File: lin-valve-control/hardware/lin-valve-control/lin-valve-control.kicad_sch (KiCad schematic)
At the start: 27 parts, among them J1 QWIIC Connector, J2 DIN-5_180degree, J3 DIN-5_180degree, J4 Screw_Terminal_01x02, J5 Screw_Terminal_01x03, J6 Screw_Terminal_01x03, Q1 2N7002, Q2 2N7002, U1 Arduino_Nano_v3.x, U2 TJA1021T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

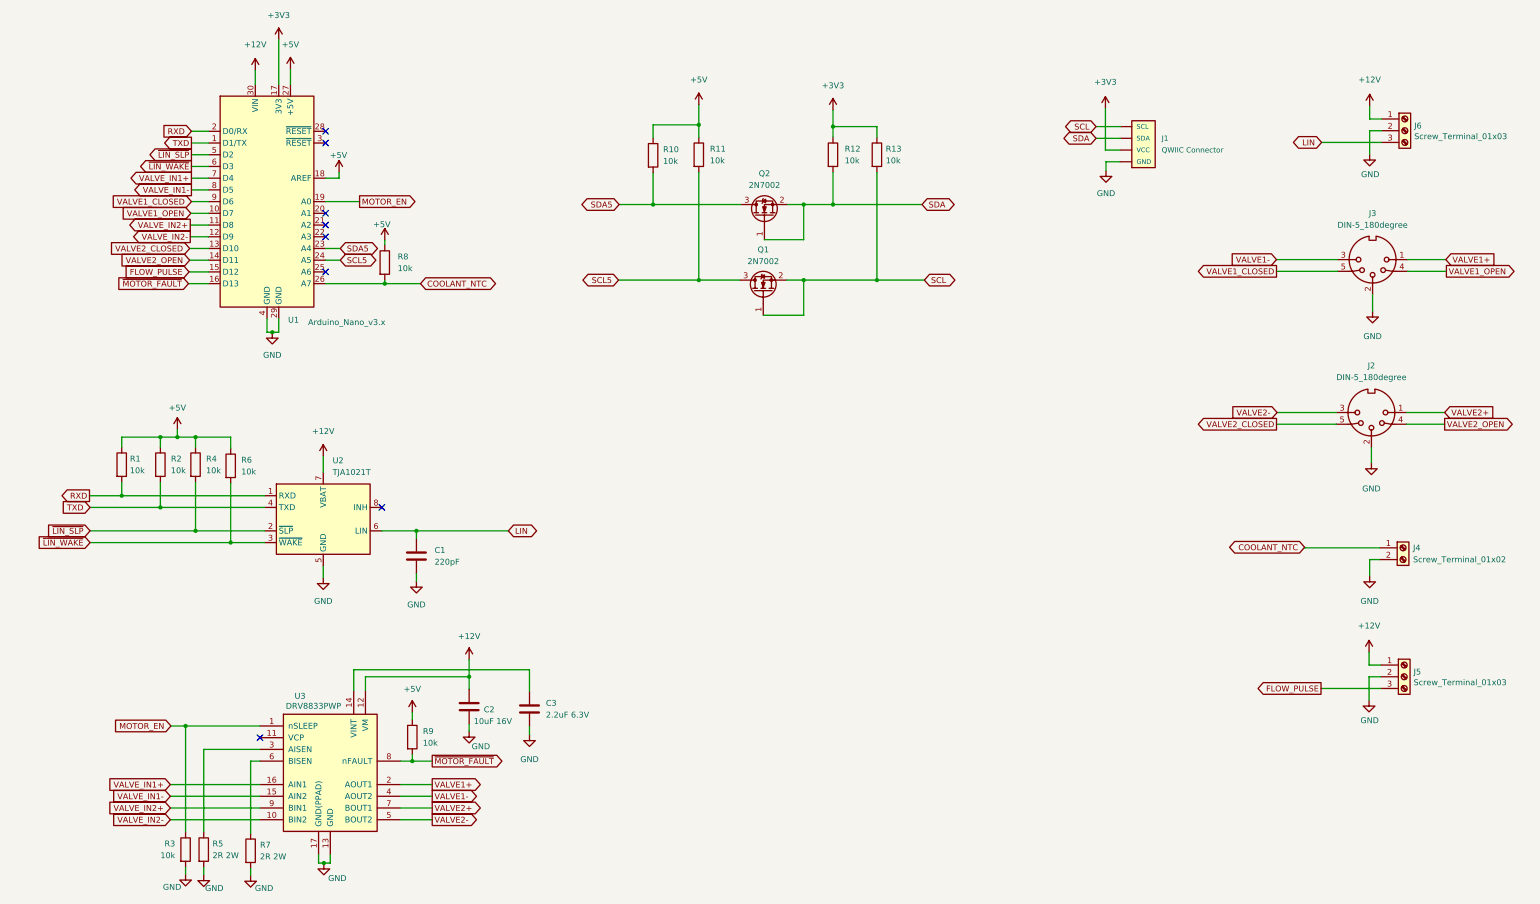
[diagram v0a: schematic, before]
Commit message: Move flow sensor to ICP1, run it at 5V
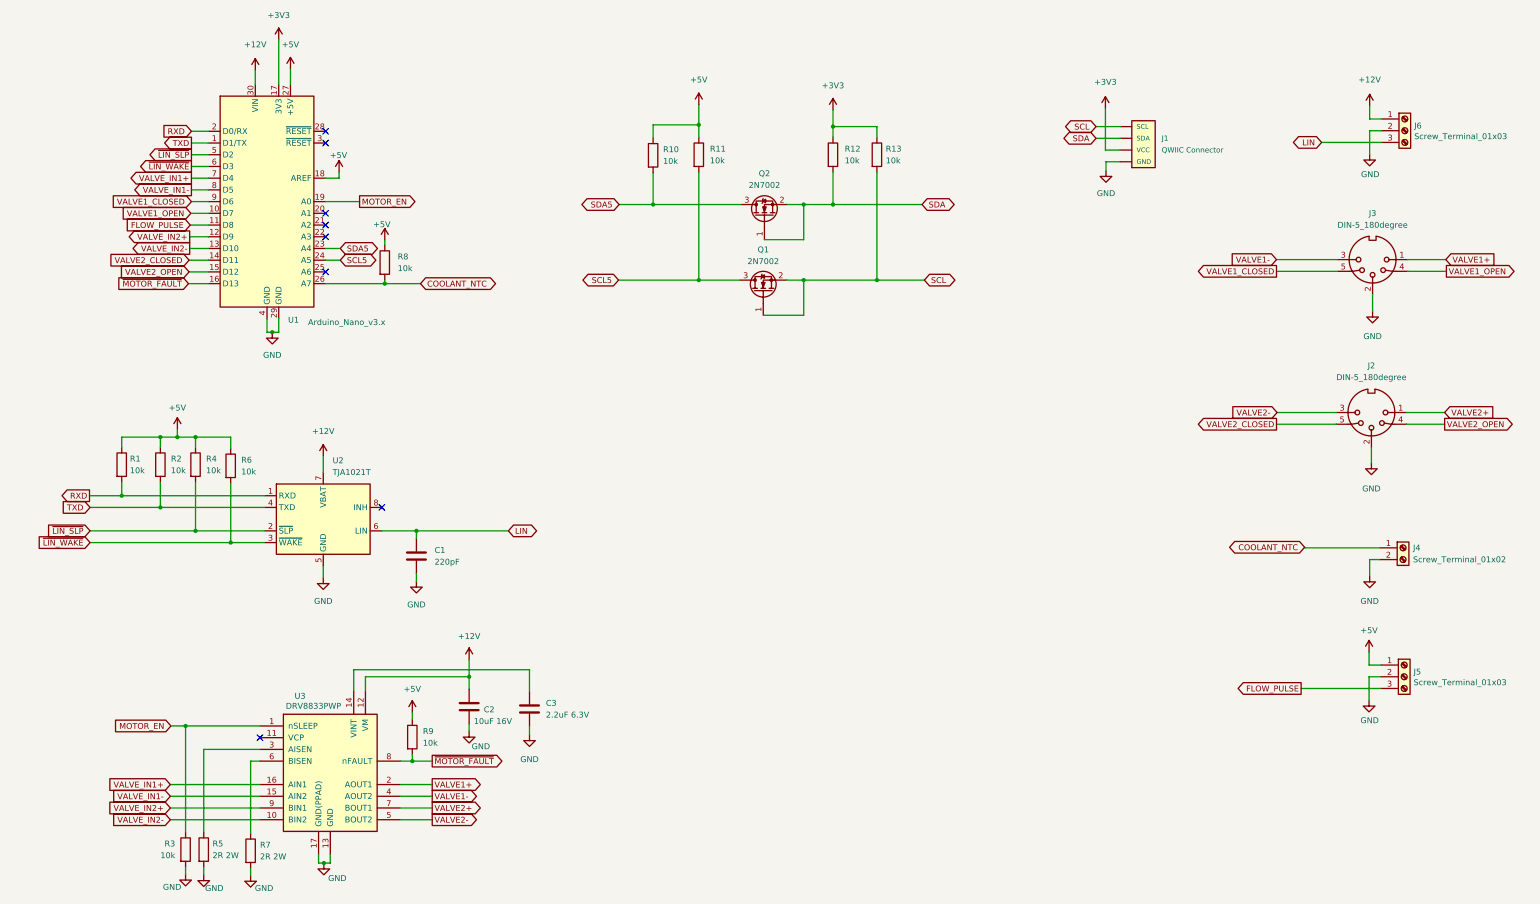
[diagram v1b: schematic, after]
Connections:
- net +12V: no longer J5.1 (Pin_1)
- net +5V: now also J5.1 (Pin_1)
- net FLOW_PULSE: now also U1.11 (D8); no longer U1.15 (D12)
- net VALVE2_CLOSED: now also U1.14 (D11); no longer U1.13 (D10)
- net VALVE2_OPEN: now also U1.15 (D12); no longer U1.14 (D11)
- net VALVE_IN2+: now also U1.12 (D9); no longer U1.11 (D8)
- net VALVE_IN2-: now also U1.13 (D10); no longer U1.12 (D9)
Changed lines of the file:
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@@
+    (stroke (width 0) (type default) (color 0 0 0 0))
+  )
+  (wire (pts (xy 48.387 67.056) (xy 52.578 67.056))
     (stroke (width 0) (type default) (color 0 0 0 0))
   )
@@
     (stroke (width 0) (type default) (color 0 0 0 0))
   )
-  (wire (pts (xy 48.641 61.976) (xy 52.578 61.976))
-    (stroke (width 0) (type default) (color 0 0 0 0))
-  )
   (wire (pts (xy 158.877 40.386) (xy 158.877 37.719))
     (stroke (width 0) (type default) (color 0 0 0 0))
@@
     (stroke (width 0) (type default) (color 0 0 0 0))
   )
-  (wire (pts (xy 306.705 159.893) (xy 293.751 159.893))
+  (wire (pts (xy 48.514 61.976) (xy 52.578 61.976))
     (stroke (width 0) (type default) (color 0 0 0 0))
   )
@@
     (stroke (width 0) (type default) (color 0 0 0 0))
   )
-  (wire (pts (xy 48.514 67.056) (xy 52.578 67.056))
-    (stroke (width 0) (type default) (color 0 0 0 0))
-  )
   (wire (pts (xy 48.895 39.116) (xy 52.578 39.116))
     (stroke (width 0) (type default) (color 0 0 0 0))
@@
   )
   (wire (pts (xy 77.978 49.276) (xy 80.899 49.276))
+    (stroke (width 0) (type default) (color 0 0 0 0))
+  )
+  (wire (pts (xy 289.433 159.893) (xy 306.705 159.893))
     (stroke (width 0) (type default) (color 0 0 0 0))
   )
@@
     )
   )
-  (global_label "VALVE_IN2-" (shape output) (at 48.641 61.976 180) (fields_autoplaced)
-    (effects (font (size 1.27 1.27)) (justify right))
-    (property "Intersheet References" "${INTERSHEET_REFS}" (id 0) (at 35.1892 61.8966 0)
+  (global_label "VALVE_IN2-" (shape output) (at 48.514 64.516 180) (fields_autoplaced)
+    (effects (font (size 1.27 1.27)) (justify right))
+    (property "Intersheet References" "${INTERSHEET_REFS}" (id 0) (at 35.0622 64.4366 0)
       (effects (font (size 1.27 1.27)) (justify right) hide)
     )
@@
     )
   )
-  (global_label "VALVE2_OPEN" (shape input) (at 48.514 67.056 180) (fields_autoplaced)
-    (effects (font (size 1.27 1.27)) (justify right))
-    (property "Intersheet References" "${INTERSHEET_REFS}" (id 0) (at 33.4898 66.9766 0)
+  (global_label "VALVE2_OPEN" (shape input) (at 48.387 69.596 180) (fields_autoplaced)
+    (effects (font (size 1.27 1.27)) (justify right))
+    (property "Intersheet References" "${INTERSHEET_REFS}" (id 0) (at 33.3628 69.5166 0)
       (effects (font (size 1.27 1.27)) (justify right) hide)
     )
@@
     )
   )
-  (global_label "VALVE2_CLOSED" (shape input) (at 48.514 64.516 180) (fields_autoplaced)
-    (effects (font (size 1.27 1.27)) (justify right))
-    (property "Intersheet References" "${INTERSHEET_REFS}" (id 0) (at 31.3127 64.4366 0)
+  (global_label "VALVE2_CLOSED" (shape input) (at 48.387 67.056 180) (fields_autoplaced)
+    (effects (font (size 1.27 1.27)) (justify right))
+    (property "Intersheet References" "${INTERSHEET_REFS}" (id 0) (at 31.1857 66.9766 0)
       (effects (font (size 1.27 1.27)) (justify right) hide)
     )
@@
     )
   )
-  (global_label "FLOW_PULSE" (shape input) (at 48.387 69.596 180) (fields_autoplaced)
-    (effects (font (size 1.27 1.27)) (justify right))
-    (property "Intersheet References" "${INTERSHEET_REFS}" (id 0) (at 34.2095 69.5166 0)
+  (global_label "FLOW_PULSE" (shape input) (at 48.641 59.436 180) (fields_autoplaced)
+    (effects (font (size 1.27 1.27)) (justify right))
+    (property "Intersheet References" "${INTERSHEET_REFS}" (id 0) (at 34.4635 59.3566 0)
       (effects (font (size 1.27 1.27)) (justify right) hide)
     )
@@
     )
   )
-  (global_label "VALVE_IN2+" (shape output) (at 48.641 59.436 180) (fields_autoplaced)
-    (effects (font (size 1.27 1.27)) (justify right))
-    (property "Intersheet References" "${INTERSHEET_REFS}" (id 0) (at 35.1892 59.3566 0)
+  (global_label "VALVE_IN2+" (shape output) (at 48.514 61.976 180) (fields_autoplaced)
+    (effects (font (size 1.27 1.27)) (justify right))
+    (property "Intersheet References" "${INTERSHEET_REFS}" (id 0) (at 35.0622 61.8966 0)
       (effects (font (size 1.27 1.27)) (justify right) hide)
     )
@@
     )
   )
-  (global_label "FLOW_PULSE" (shape output) (at 293.751 159.893 180) (fields_autoplaced)
-    (effects (font (size 1.27 1.27)) (justify right))
-    (property "Intersheet References" "${INTERSHEET_REFS}" (id 0) (at 279.5735 159.8136 0)
+  (global_label "FLOW_PULSE" (shape output) (at 289.433 159.893 180) (fields_autoplaced)
+    (effects (font (size 1.27 1.27)) (justify right))
+    (property "Intersheet References" "${INTERSHEET_REFS}" (id 0) (at 275.2555 159.8136 0)
       (effects (font (size 1.27 1.27)) (justify right) hide)
     )
@@
     )
     (property "Datasheet" "" (id 3) (at 247.142 47.625 0)
-      (effects (font (size 1.27 1.27)) hide)
-    )
-    (pin "1")
-  )
-  (symbol (lib_id "power:+12V") (at 304.165 152.019 0) (unit 1)
-    (in_bom yes) (on_board yes) (fields_autoplaced)
-    (property "Reference" "#PWR023" (id 0) (at 304.165 155.829 0)
-      (effects (font (size 1.27 1.27)) hide)
-    )
-    (property "Value" "+12V" (id 1) (at 304.165 146.304 0))
-    (property "Footprint" "" (id 2) (at 304.165 152.019 0)
-      (effects (font (size 1.27 1.27)) hide)
-    )
-    (property "Datasheet" "" (id 3) (at 304.165 152.019 0)
       (effects (font (size 1.27 1.27)) hide)
     )
@@
     (pin "1")
   )
+  (symbol (lib_id "power:+5V") (at 304.165 152.019 0) (unit 1)
+    (in_bom yes) (on_board yes) (fields_autoplaced)
+    (property "Reference" "#PWR?" (id 0) (at 304.165 155.829 0)
+      (effects (font (size 1.27 1.27)) hide)
+    )
+    (property "Value" "+5V" (id 1) (at 304.165 147.32 0))
+    (property "Footprint" "" (id 2) (at 304.165 152.019 0)
+      (effects (font (size 1.27 1.27)) hide)
+    )
+    (property "Datasheet" "" (id 3) (at 304.165 152.019 0)
+      (effects (font (size 1.27 1.27)) hide)
+    )
+    (pin "1")
+  )
   (sheet_instances
     (path "/" (page "1"))
@@
       (reference "#PWR022") (unit 1) (value "GND") (footprint "")
     )
-    (path "/9355cddc-26ed-4b85-80d8-5d44afb584f9"
-      (reference "#PWR023") (unit 1) (value "+12V") (footprint "")
-    )
     (path "/2b15dcfc-1520-4124-aba9-0f440be5bf33"
       (reference "#PWR024") (unit 1) (value "GND") (footprint "")
@@
       (reference "#PWR029") (unit 1) (value "GND") (footprint "")
     )
+    (path "/fc94f245-2b8d-436c-b091-f7150042f6eb"
+      (reference "#PWR?") (unit 1) (value "+5V") (footprint "")
+    )
     (path "/c0e53e62-f89d-41ff-91b0-9eb5efa0a511"
